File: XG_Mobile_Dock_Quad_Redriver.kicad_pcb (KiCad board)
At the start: 6 copper layers, 220.1 x 93 mm, 225 parts, among them J1 5-1775443-8, J10 SWD, J11 UART, J12 I2C1, J13 39301240, J14 I2C1, J2 20455-040E-76, J3 20455-040E-76, J4 469911008, J7 CEE016400140111, Q16 AO3401A, Q17 2N7002W, SW1 SW_Push, U1 DS160PR410RNQR, U12 STM32F030C8Tx, U2 DS160PR410RNQR, U6 DS160PR410RNQR, U7 TPS7A8400ARGRR, U8 TPS7A8400ARGRR, U9 DS160PR410RNQR

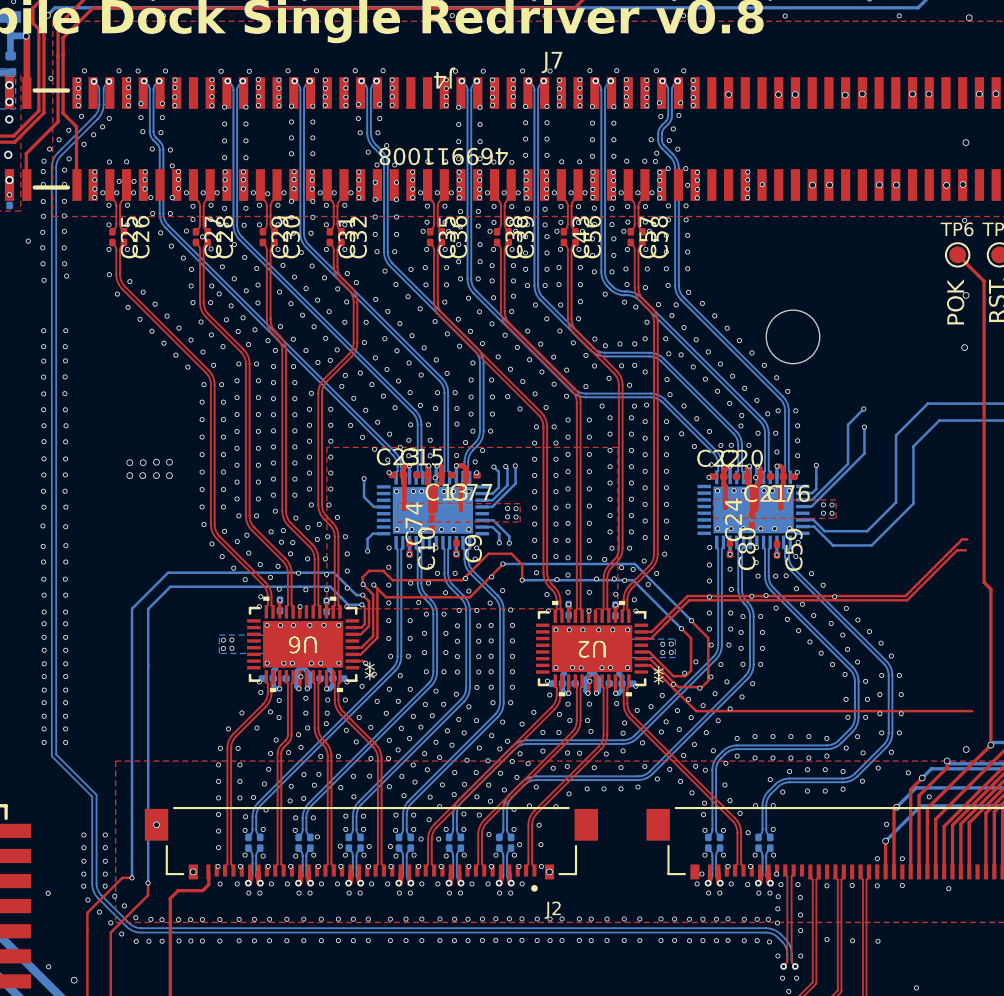
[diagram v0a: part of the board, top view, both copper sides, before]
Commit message: Quad redriver: via fence at consistent 0.21mm clearance (drop channel centering; 1113 GND vias)
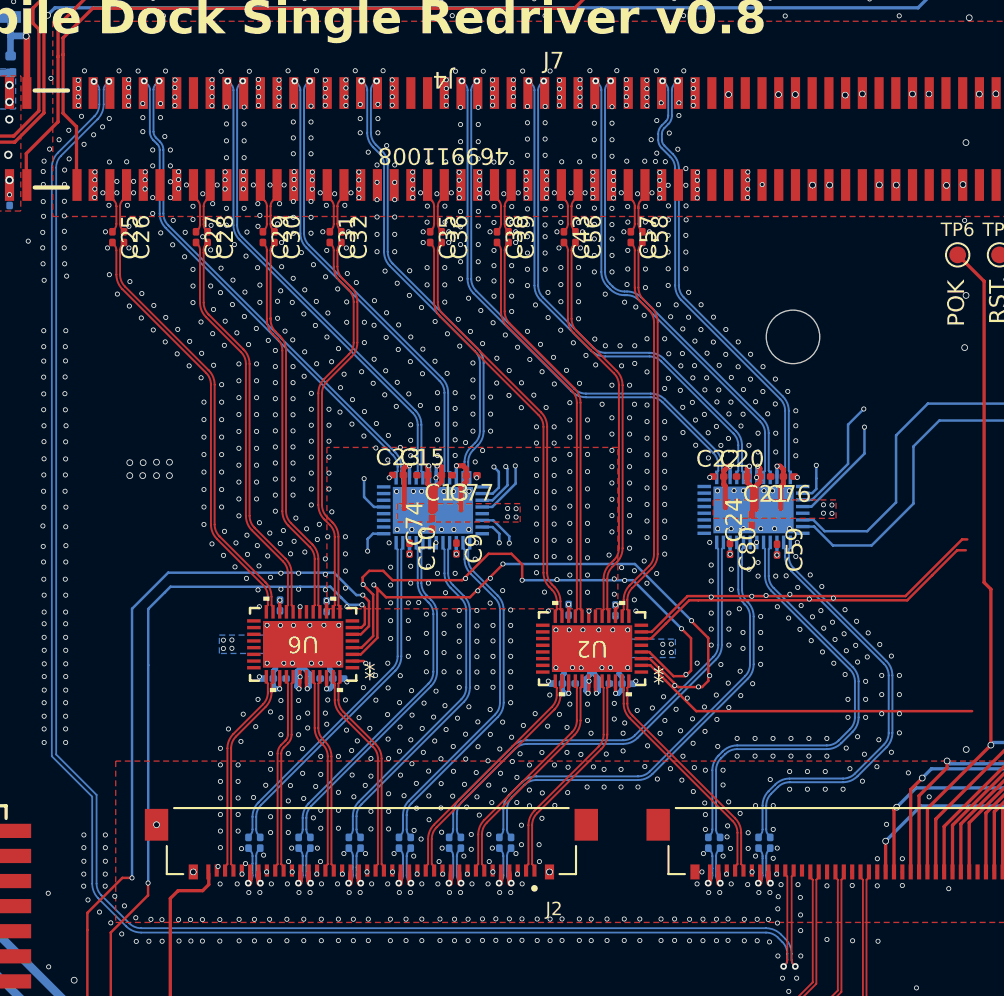
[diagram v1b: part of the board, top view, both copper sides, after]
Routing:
- net GND: vias 2100 -> 2147
